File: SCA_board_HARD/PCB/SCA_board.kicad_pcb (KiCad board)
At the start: 2 copper layers, 30.1 x 128 mm, 26 parts, among them J1 100616-2, J2 39-29-3086, J3 DIN41612_02x32_AC, J4 USB4145-03-0230-C, J6 USB4145-03-0230-C, J7 Conn_01x03, U1 USBLC6-2SC6, U2 CH340E

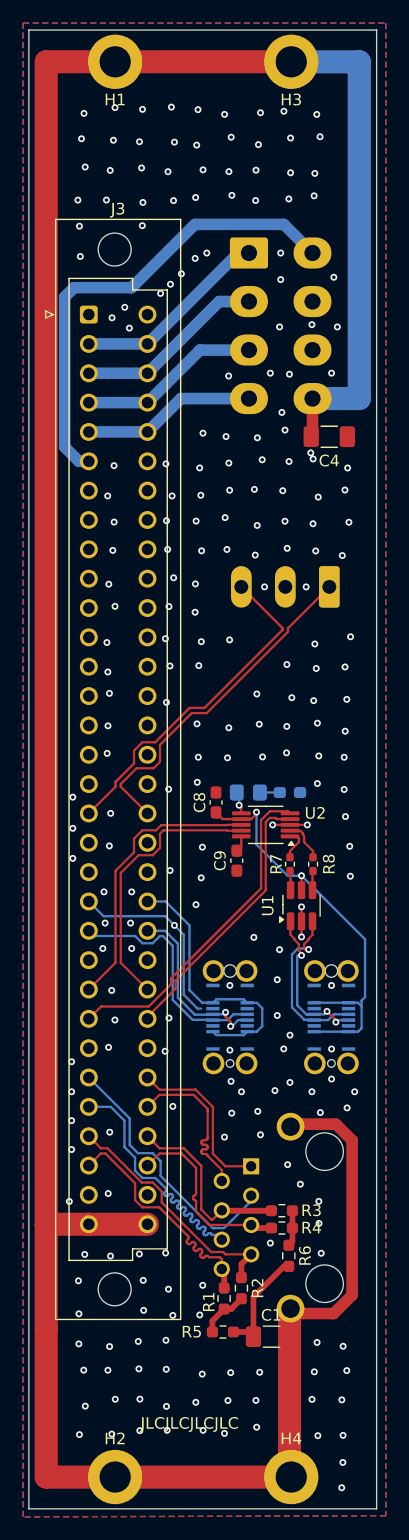
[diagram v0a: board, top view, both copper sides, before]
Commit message: Added i2c config eeprom and testpoints
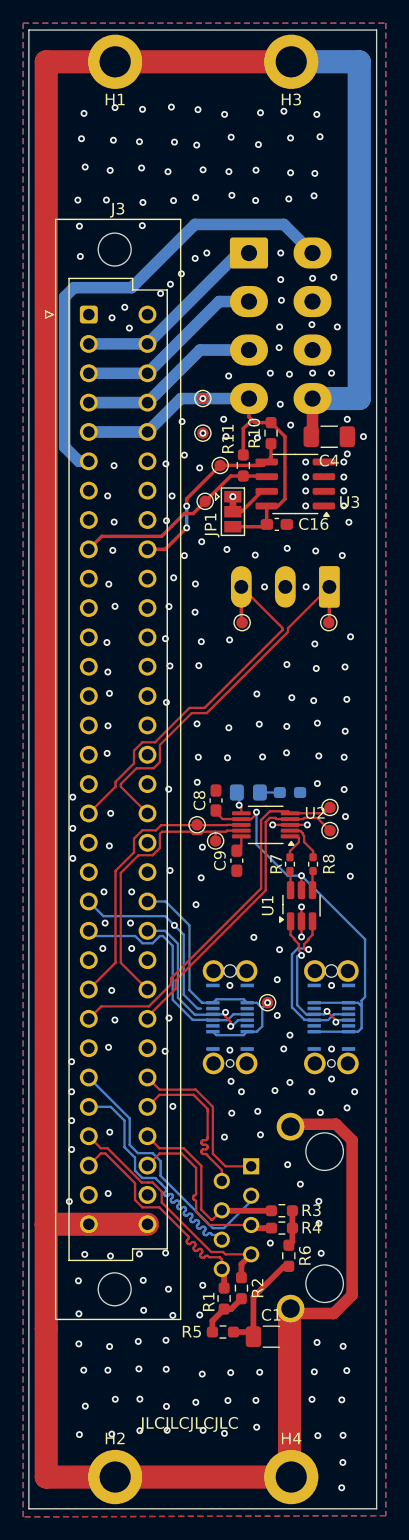
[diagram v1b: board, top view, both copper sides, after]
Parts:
- added C16: 100n, Capacitor_SMD:C_0603_1608Metric_Pad1.08x0.95mm_HandSolder, F.Cu at (147.4, 75.6)
- added JP1: SolderJumper_3_Bridged12, Jumper:SolderJumper-3_P1.3mm_Bridged12_Pad1.0x1.5mm, F.Cu at (143.6, 74.5)
- added R10: 10k, Resistor_SMD:R_0603_1608Metric_Pad0.98x0.95mm_HandSolder, F.Cu at (146.9, 67.7)
- added R11: 10k, Resistor_SMD:R_0603_1608Metric_Pad0.98x0.95mm_HandSolder, F.Cu at (144.5, 70.5)
- added TP1: TestPoint, TestPoint:TestPoint_Pad_D1.0mm, F.Cu at (142.5, 70.5)
- added TP10: TestPoint, TestPoint:TestPoint_Pad_D1.0mm, F.Cu at (144.4, 84.1)
- added TP11: TestPoint, TestPoint:TestPoint_Pad_D1.0mm, F.Cu at (141.0, 64.7)
- added TP2: TestPoint, TestPoint:TestPoint_Pad_D1.0mm, F.Cu at (141.2, 73.6)
- added TP3: TestPoint, TestPoint:TestPoint_Pad_D1.0mm, F.Cu at (146.6, 117.0)
- added TP4: TestPoint, TestPoint:TestPoint_Pad_D1.0mm, F.Cu at (141.0, 67.7)
- added TP5: TestPoint, TestPoint:TestPoint_Pad_D1.0mm, F.Cu at (140.5, 101.6)
- added TP6: TestPoint, TestPoint:TestPoint_Pad_D1.0mm, F.Cu at (142.1, 103.0)
- added TP7: TestPoint, TestPoint:TestPoint_Pad_D1.0mm, F.Cu at (152.0, 100.1)
- added TP8: TestPoint, TestPoint:TestPoint_Pad_D1.0mm, F.Cu at (152.0, 102.1)
- added TP9: TestPoint, TestPoint:TestPoint_Pad_D1.0mm, F.Cu at (151.9, 84.1)
- added U3: M24C02-WMN, Package_SO:SOIC-8_3.9x4.9mm_P1.27mm, F.Cu at (149.0, 72.1)
- moved C8 0.17 mm to (142.1, 99.5)
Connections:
- J3 pad a10: unconnected-(J3-Pin_a10-Pada10) -> GND
- J3 pad a9: unconnected-(J3-Pin_a9-Pada9) -> /SCL
- J3 pad c10: unconnected-(J3-Pin_c10-Padc10) -> GND
- J3 pad c9: unconnected-(J3-Pin_c9-Padc9) -> /SDA
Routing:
- net /+3,3V_CONN: track 15.1 -> 35.7 mm, vias 0 -> 1
- net /SCL: track 0.00 -> 18.0 mm
- net /SDA: track 0.00 -> 16.7 mm, vias 0 -> 2
- net /RTS: track 23.6 -> 27.5 mm
- net /CTS: track 28.7 -> 32.4 mm
- net Net-(JP1-C): track 0.00 -> 3.66 mm
- net /RS485-: track 29.5 -> 32.6 mm
- net /RS485+: track 29.7 -> 32.8 mm
- net /USART+: track 23.7 -> 24.7 mm
- net /VUSB: track 23.6 -> 24.2 mm, vias 0 -> 1
- net GND: vias 251 -> 253
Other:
- board text added: "GND"
